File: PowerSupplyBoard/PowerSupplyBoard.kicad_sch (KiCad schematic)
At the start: 70 parts, among them J101 BATTERY, J102 POWER, J103 USB_C, J104 PWR, J105 DATA, Q101 BSH205G2A, Q102 TD6790, Q103 TD6790, Q104 TD6790, U101 TPS63021, U102 MCP73834T, U103 TC7662Bx0A, U104 TC7662Bx0A, U105 CS5173

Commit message: Power Supply rev2
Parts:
- added D108: PMEG3030, Diode_SMD:D_SOD-123, symbol Device:D_Schottky
- added D109, D110: SP0503BAHT, Package_TO_SOT_SMD:SOT-143, symbol Power_Protection:SP0503BAHT
- added J106: USB_B_Micro, Connector_USB:USB_Micro-B_Amphenol_10118193-0001LF_Horizontal, symbol Connector:USB_B_Micro
- added R115: LOOP, Resistor_THT:R_Axial_DIN0204_L3.6mm_D1.6mm_P5.08mm_Horizontal, symbol Device:R_US
- added SW101: SW_SPDT, Button_Switch_THT:SW_NKK_B12JH_SPDT, symbol Switch:SW_SPDT
- J102: value POWER -> DATA2
- J103: footprint Connector_USB:USB_C_Receptacle_JAE_DX07S016JA1R1500 -> Connector_USB:USB_C_Receptacle_Palconn_UTC16-G
- J105: value DATA -> DATA1
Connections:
- net GND: now also D109.1 (A), D110.1 (A), J106.5 (GND), J106.6 (Shield), R115.1, R115.2
- net VCC: now also SW101.2 (B); no longer J102.1 (Pin_1)
- net VDD: now also D108.1 (K)
- net VIN: now also SW101.1 (A); no longer J102.2 (Pin_2)
- net at D107.2 (A), J103.A4 (VBUS), J103.A9 (VBUS)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: now also D109.2 (K)
- net USB_D+ renamed USBC_D+
- net USBC_D+: now also J105.2 (Pin_2), D109.3 (K); no longer J105.1 (Pin_1)
- net USB_D- renamed USBC_D-
- net USBC_D-: now also J105.1 (Pin_1), D109.4 (K); no longer J105.2 (Pin_2)
- new net: D108.2 (A), D110.4 (K), J106.1 (VBUS)
- new net USBM_D+: D110.3 (K), J102.1 (Pin_1), J106.3 (D+)
- new net USBM_D-: D110.2 (K), J102.2 (Pin_2), J106.2 (D-)
- no-connect marks 7 -> 9
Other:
- note added: "Parallel charge pumps share output cap C113 as shown in fig. 5 of the datasheet. Between the two we can sink ~80mA."
- note added: "USB Connectors"
- note removed: "Parallel charge pumps share output cap C713 as shown in fig. 5 of the datasheet. Between the two we can sink ~80mA."
- note removed: "USB C Connector"
- moved on the sheet: J104, J105

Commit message: Power supply rev2 gerbers
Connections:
- net USBC_D+: now also D109.2 (K); no longer D109.3 (K)
- net USBC_D-: now also D109.3 (K); no longer D109.4 (K)
- net at D107.2 (A), J103.A4 (VBUS), J103.A9 (VBUS)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: now also D109.4 (K); no longer D109.2 (K)
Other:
- moved on the sheet: D107

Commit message: AD5280 driver
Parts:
- removed C111, C112, C113: 10u, Capacitor_SMD:C_0805_2012Metric, symbol Device:C
- removed JP102, JP103: INV_HIFREQ, Jumper:SolderJumper-2_Open_TrianglePad_0805, symbol Jumper:SolderJumper_2_Open
- removed TP104: -12A, TestPoint:TestPoint_Pad_D1.0mm_Value, symbol Connector:TestPoint
- removed U103, U104: TC7662Bx0A, Package_DIP:DIP-8_W7.62mm, symbol Converter_DCDC:TC7662Bx0A
- added U103: MAX17578ATC, Package_DFN_QFN:TDFN-12-1EP_3x3mm_P0.4mm_EP1.7x2.45mm, symbol Regulator_Switching:MAX17578ATC
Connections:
- no-connect marks 9 -> 5
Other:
- note removed: "JP701 and 702 can be shorted to increase the internal osc frequency if desired"
- note removed: "Parallel charge pumps share output cap C113 as shown in fig. 5 of the datasheet. Between the two we can sink ~80mA."

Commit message: Power board rev 3
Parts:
- removed C117, C118: 1u, Capacitor_SMD:C_0805_2012Metric, symbol Device:C
- removed C119, C120: 100n, Capacitor_SMD:C_0805_2012Metric, symbol Device:C
- removed D108: PMEG3030, Diode_SMD:D_SOD-123, symbol Device:D_Schottky
- removed D110: SP0503BAHT, Package_TO_SOT_SMD:SOT-143, symbol Power_Protection:SP0503BAHT
- removed J102: DATA2, Connector_PinHeader_2.54mm:PinHeader_1x02_P2.54mm_Vertical, symbol Connector:Conn_01x02_Pin
- removed J106: USB_B_Micro, Connector_USB:USB_Micro-B_Amphenol_10118193-0001LF_Horizontal, symbol Connector:USB_B_Micro
- removed JP101: DIG_CM, Jumper:SolderJumper-2_Open_TrianglePad_0805, symbol Jumper:SolderJumper_2_Open
- removed JP104: POS_CM, Jumper:SolderJumper-2_Open_TrianglePad_0805, symbol Jumper:SolderJumper_2_Open
- removed JP105: NEG_CM, Jumper:SolderJumper-2_Open_TrianglePad_0805, symbol Jumper:SolderJumper_2_Open
- removed Q102, Q103, Q104: TD6790, PCM_4ms_Package_SOIC:SM-8, symbol Transistor_BJT:TD6790
- removed TP106: -12V, TestPoint:TestPoint_Pad_D1.0mm_Value, symbol Connector:TestPoint
- removed TP107: +12V, TestPoint:TestPoint_Pad_D1.0mm_Value, symbol Connector:TestPoint
- added C111: 4u7, Capacitor_SMD:C_0805_2012Metric, symbol Device:C
- added C112: 4n7, Capacitor_SMD:C_0805_2012Metric, symbol Device:C
- added C113: 2u2, Capacitor_SMD:C_0805_2012Metric, symbol Device:C
- added L103: 22uH, Inductor_SMD:L_Changjiang_FNR4010S, symbol Device:L
- added R116: 330k, Resistor_SMD:R_0805_2012Metric, symbol Device:R_US
- added R117: 100k, Resistor_SMD:R_0805_2012Metric, symbol Device:R_US
- added RV101, RV102: 10k, Potentiometer_THT:Potentiometer_Bourns_3296W_Vertical, symbol Device:R_Potentiometer_Trim_US
- C103: value 22u -> 100n
- C107: value 100n -> 22u
- R103: value 10k -> 1k
- R111: value 4k7 -> 470k
- R112: value 12k -> 33k
- R113: value 12k -> 4k7
- TP101: value 3V3 -> -12
- TP102: value 3V3P -> 3V3
- TP105: value +12A -> +12
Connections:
- net +12V: now also C116.1, D106.1 (K), R110.1, TP105.1, U103.1 (VIN), C111.1, R116.1
- net +3.3V: now also C108.1, R105.1, R113.2, TP102.1, U101.3 (FB), U101.4 (VOUT), U101.5 (VOUT); no longer C107.1, TP101.1
- net -12V: now also C107.2, R112.2, TP101.1, U103.12 (VOUT), U103.13 (EP), U103.8 (SOUT), C112.2, C113.2
- net GND: now also C107.1, R103.2, R111.1, U103.9 (GND), C111.2, L103.2, R117.2; no longer C103.2, C107.2, R111.2
- net at U103.10 (BST): now also C103.1
- net at U103.11 (LX): now also C103.2, L103.1
- net at U103.2 (EN/UVLO): now also R116.2, R117.1
- net NRST: now reaches U103.3 (~{RST})
- net NRST: now also R113.1
- net at U103.4 (SS): now also C112.1
- net at U103.5 (VCC): now also C113.1
- net at U103.7 (FB): now also R111.2, RV102.1
- net at R110.2, U105.2 (FB): now also RV101.1; no longer R111.1
- removed net +12VA: C116.1, D106.1 (K), R110.1, R113.1, TP105.1
- removed net +3.3VP: C108.1, R103.1, R105.1, TP102.1, U101.3 (FB), U101.4 (VOUT), U101.5 (VOUT)
- net -12VA: no longer names the net of R112.1
- net -12VA: now also RV102.2, RV102.3
- new net: R103.1, RV101.2, RV101.3
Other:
- note added: "USB Connector"
- note removed: "BJT capacitance multipliers"
- note removed: "These capacitance multipliers should smooth the power lines to <1mV of ripple when populated, if not they can be bypassed with solder jumpers"
- note removed: "USB Connectors"
- moved on the sheet: C101, C102, C104, C105, C106, C108, C109, C110, C114, C115, C116, D101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

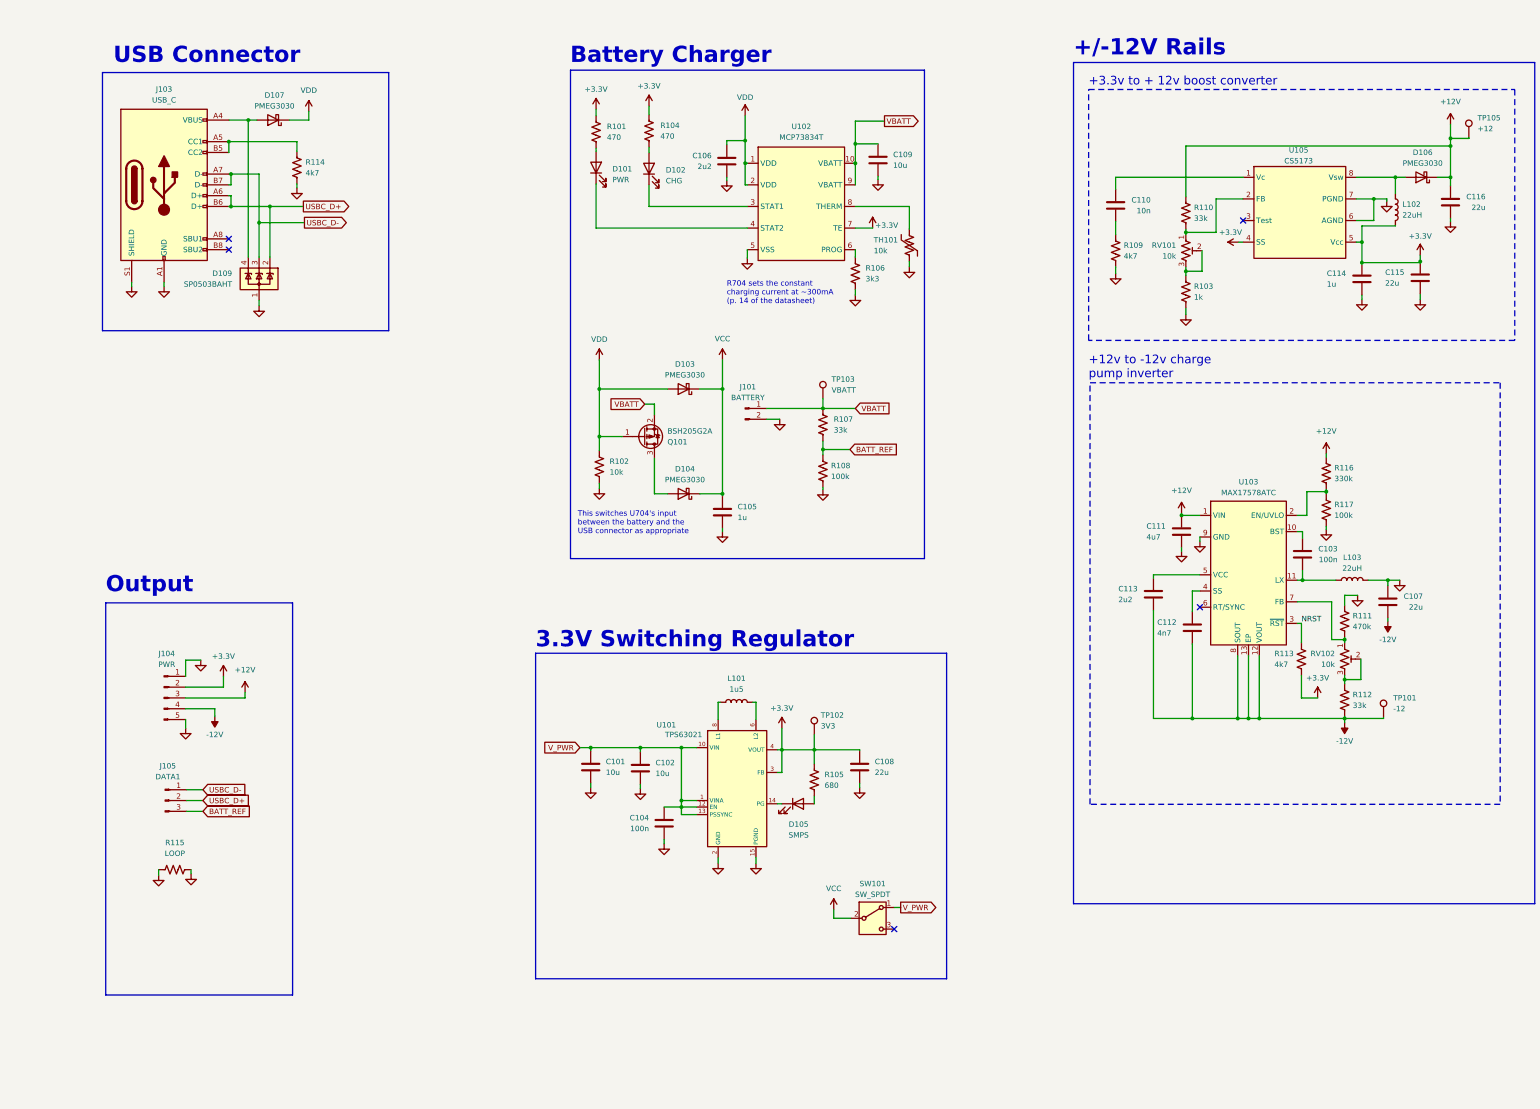
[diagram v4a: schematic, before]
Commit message: PSU rev4 schematic
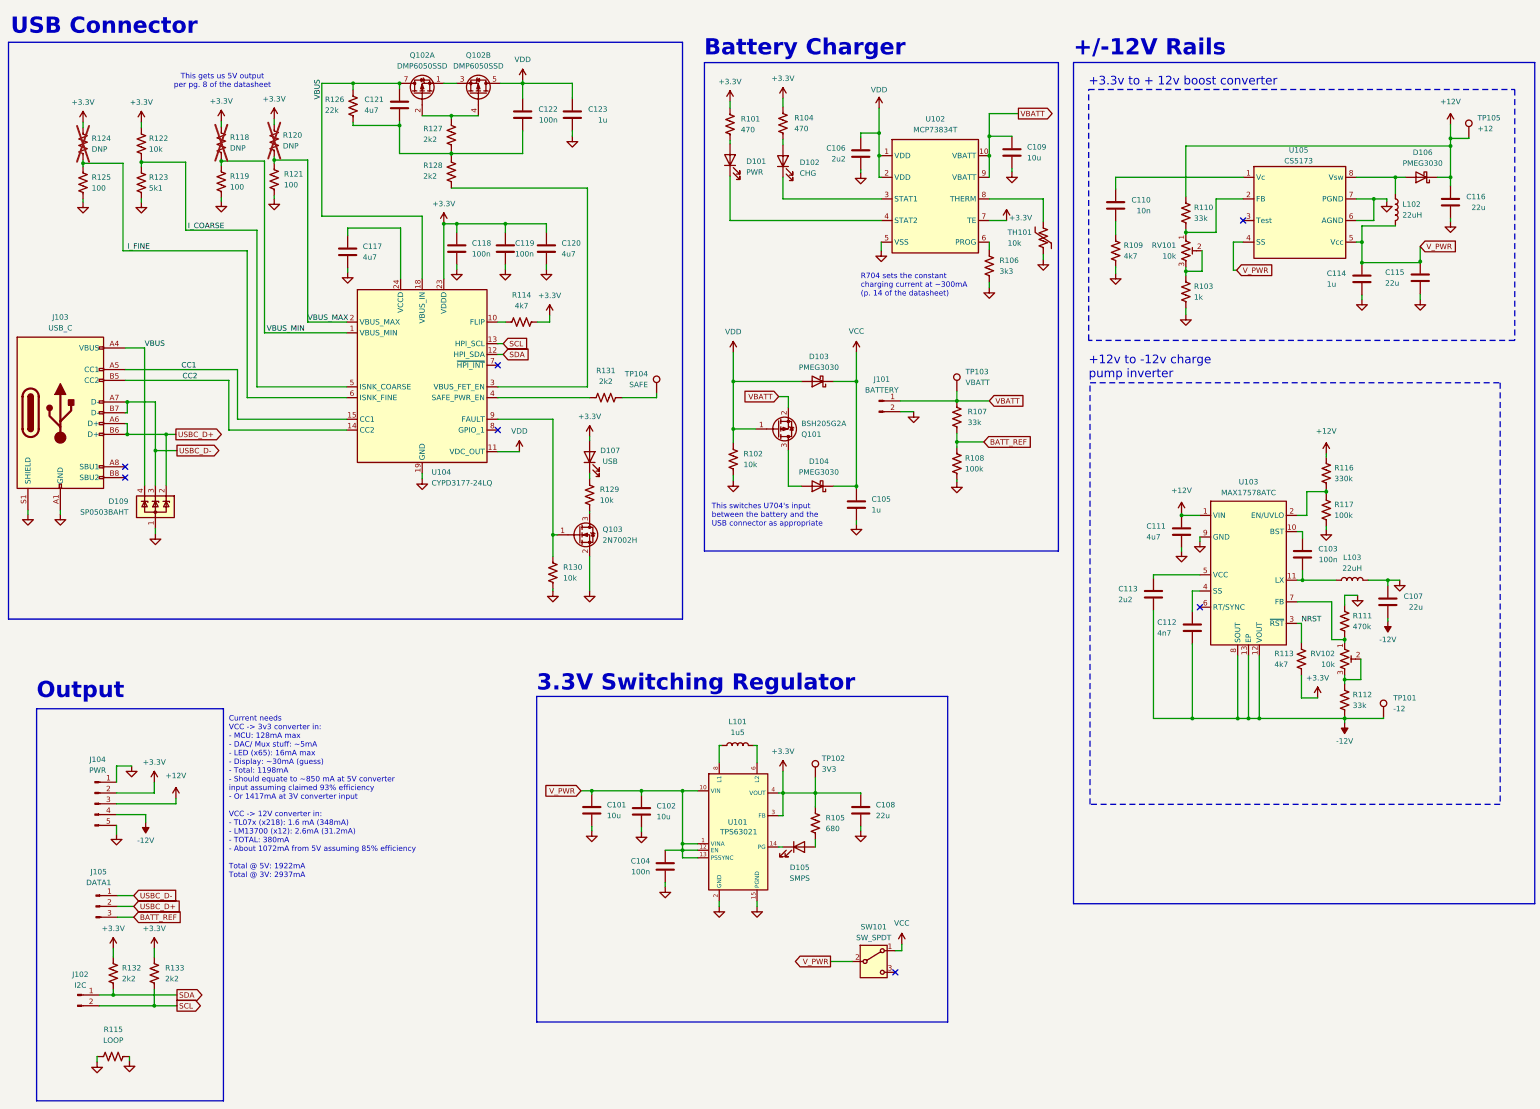
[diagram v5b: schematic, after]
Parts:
- removed D107: PMEG3030, Diode_SMD:D_SOD-123, symbol Device:D_Schottky
- added C117, C120, C121: 4u7, Capacitor_SMD:C_0805_2012Metric, symbol Device:C
- added C118, C119, C122: 100n, Capacitor_SMD:C_0805_2012Metric, symbol Device:C
- added C123: 1u, Capacitor_SMD:C_0805_2012Metric, symbol Device:C
- added D107: USB, LED_THT:LED_D3.0mm, symbol Device:LED
- added J102: I2C, Connector_PinHeader_2.54mm:PinHeader_1x02_P2.54mm_Vertical, symbol Connector:Conn_01x02_Pin
- added Q102: DMP6050SSD, Package_SO:SOIC-8_3.9x4.9mm_P1.27mm, symbol Transistor_FET:DMP6050SSD
- added Q103: 2N7002H, Package_TO_SOT_SMD:SOT-23, symbol Transistor_FET:2N7002H
- added R118, R120, R124: DNP, Resistor_SMD:R_0805_2012Metric, symbol Device:R_US
- added R119, R121, R125: 100, Resistor_SMD:R_0805_2012Metric, symbol Device:R_US
- added R122, R129, R130: 10k, Resistor_SMD:R_0805_2012Metric, symbol Device:R_US
- added R123: 5k1, Resistor_SMD:R_0805_2012Metric, symbol Device:R_US
- added R126: 22k, Resistor_SMD:R_0805_2012Metric, symbol Device:R_US
- added R127, R128, R131, R132, R133: 2k2, Resistor_SMD:R_0805_2012Metric, symbol Device:R_US
- added TP104: SAFE, TestPoint:TestPoint_THTPad_D1.0mm_Drill0.5mm_VAL, symbol Connector:TestPoint
- added U104: CYPD3177-24LQ, Package_DFN_QFN:QFN-24-1EP_4x4mm_P0.5mm_EP2.75x2.75mm, symbol Interface_USB:CYPD3177-24LQ
- TP101, TP102, TP103, TP105: footprint TestPoint:TestPoint_Pad_D1.0mm_Value -> TestPoint:TestPoint_THTPad_D1.0mm_Drill0.5mm_VAL
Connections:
- net +3.3V: now also R114.2, C118.1, C119.1, C120.1, D107.2 (A), R118.1, R120.1, R122.1, R124.1, R132.1, R133.1, U104.23 (VDDD); no longer C114.1, C115.1, L102.2, U105.4 (SS), U105.5 (Vcc)
- net GND: now also C117.2, C118.2, C119.2, C120.2, C123.2, Q103.2 (S), R119.2, R121.2, R123.2, R125.2, R130.2, U104.19 (GND), U104.22 (GND), U104.25 (GND); no longer R114.2
- net VCC: now also SW101.1 (A); no longer SW101.2 (B)
- net VDD: now also C122.1, C123.1, Q102.5 (D2), Q102.6 (D2), U104.11 (VDC_OUT)
- net VIN: now also C114.1, C115.1, L102.2, SW101.2 (B), U105.4 (SS), U105.5 (Vcc); no longer SW101.1 (A)
- net VBUS: now reaches D109.4 (K), J103.A4 (VBUS), J103.A9 (VBUS), J103.B4 (VBUS), J103.B9 (VBUS)
- net VBUS: now also C121.1, Q102.7 (D1), Q102.8 (D1), R126.1, U104.18 (VBUS_IN)
- new net: C121.2, C122.2, R126.2, R127.2, R128.1
- new net: R114.1, U104.10 (FLIP)
- new net: C117.1, U104.24 (VCCD)
- new net: R128.2, U104.3 (VBUS_FET_EN)
- new net: R131.1, U104.4 (SAFE_PWR_EN)
- new net: Q103.1 (G), R130.1, U104.9 (FAULT)
- new net: R131.2, TP104.1
- new net: Q102.1 (S1), Q102.3 (S2)
- new net: Q102.2 (G1), Q102.4 (G2), R127.1
- new net: Q103.3 (D), R129.2
- new net: D107.1 (K), R129.1
- new net CC1: J103.A5 (CC1), U104.15 (CC1)
- new net CC2: J103.B5 (CC2), U104.14 (CC2)
- new net I_COARSE: R122.2, R123.1, U104.5 (ISNK_COARSE)
- new net I_FINE: R124.2, R125.1, U104.6 (ISNK_FINE)
- new net SCL: J102.2 (Pin_2), R133.2, U104.13 (HPI_SCL)
- new net SDA: J102.1 (Pin_1), R132.2, U104.12 (HPI_SDA)
- new net VBUS_MAX: R120.2, R121.1, U104.2 (VBUS_MAX)
- new net VBUS_MIN: R118.2, R119.1, U104.1 (VBUS_MIN)
- no-connect marks 5 -> 7
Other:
- note added: "Current needs VCC -> 3v3 converter in: - MCU: 128mA max - DAC/ Mux stuff: ~5mA - LED (x65): 16mA max - Display: ~30mA (guess) - Total: 1198mA - Should equate to ~850 mA at 5V converter input assuming claimed 93% efficiency - Or 1417mA at 3V converter input VCC -> 12V converter in: - TL07x (x218): 1.6 mA (348mA) - LM13700 (x12): 2.6mA (31.2mA) - TOTAL: 380mA - About 1072mA from 5V assuming 85% eff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"
- note added: "This gets us 5V output per pg. 8 of the datasheet"
- moved on the sheet: C101, C102, C104, C105, C106, C108, C109, D101, D102, D103, D104, D105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

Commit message: routing v1
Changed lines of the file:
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@@
-	)
-	(junction
-		(at 354.33 44.45)
-		(diameter 0)
-		(color 0 0 0 0)
 	)
 	(junction
@@
 	(wire
 		(pts
-			(xy 354.33 44.45) (xy 354.33 46.228)
-		)
-		(stroke
-			(width 0)
-			(type default)
-		)
-	)
-	(wire
-		(pts
 			(xy 292.1 46.228) (xy 354.33 46.228)
 		)
@@
 	(wire
 		(pts
-			(xy 358.648 44.45) (xy 354.33 44.45)
+			(xy 358.648 46.228) (xy 354.33 46.228)
 		)
 		(stroke
@@
 	(wire
 		(pts
-			(xy 354.33 41.148) (xy 354.33 44.45)
-		)
-		(stroke
-			(width 0)
-			(type default)
-		)
-	)
-	(wire
-		(pts
 			(xy 251.206 51.562) (xy 251.206 52.324)
 		)
@@
 	(wire
 		(pts
-			(xy 358.648 44.196) (xy 358.648 44.45)
+			(xy 358.648 44.196) (xy 358.648 46.228)
 		)
 		(stroke
@@
 		)
 		(stroke
+			(width 0)
+			(type default)
+		)
+	)
+	(wire
+		(pts
+			(xy 354.33 41.148) (xy 354.33 46.228)
+		)
+		(stroke
